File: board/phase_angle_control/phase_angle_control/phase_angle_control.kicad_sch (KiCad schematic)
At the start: 34 parts, among them J1 Screw_Terminal_01x03, J2 Conn_02x04_Odd_Even, J3 A2541HWV-7P, J4 Screw_Terminal_01x02, J6 Conn_02x04_Odd_Even, M1 MountingHoles, T1 Transformer_1P_1S, U1 STM32G030F6P, U2 EL354N(A)(TA)-VG, U3 MOC3052S-TA1, U4 ACS758xCB-050B-PFF

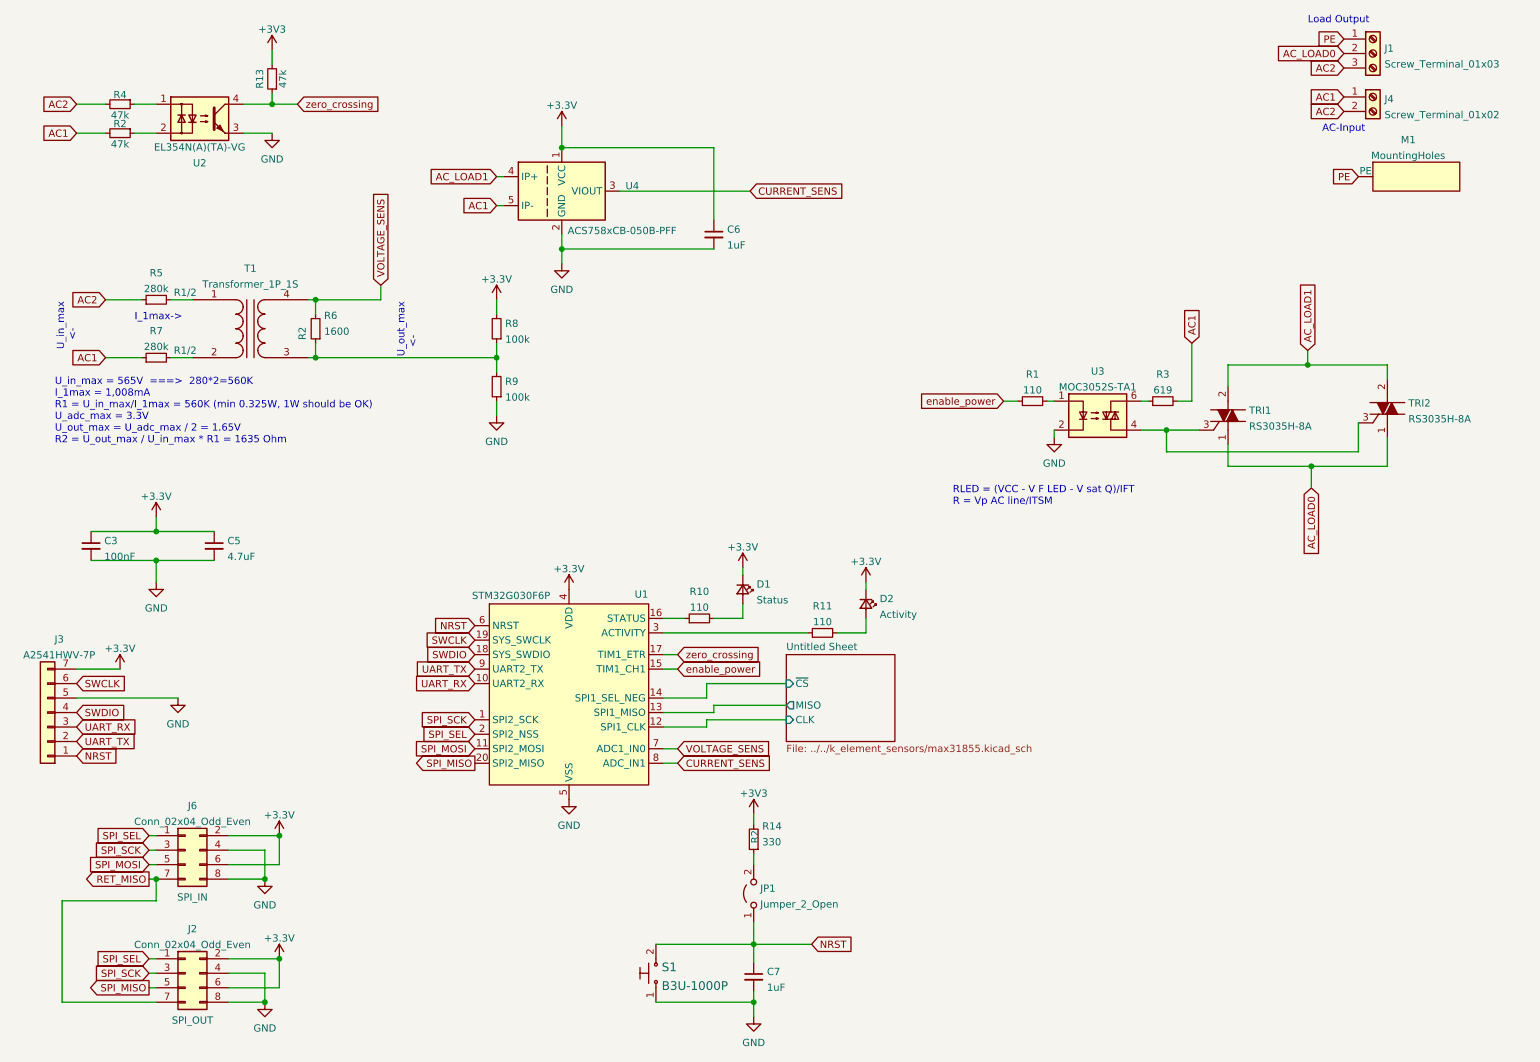
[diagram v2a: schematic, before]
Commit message: Fix LED rotation
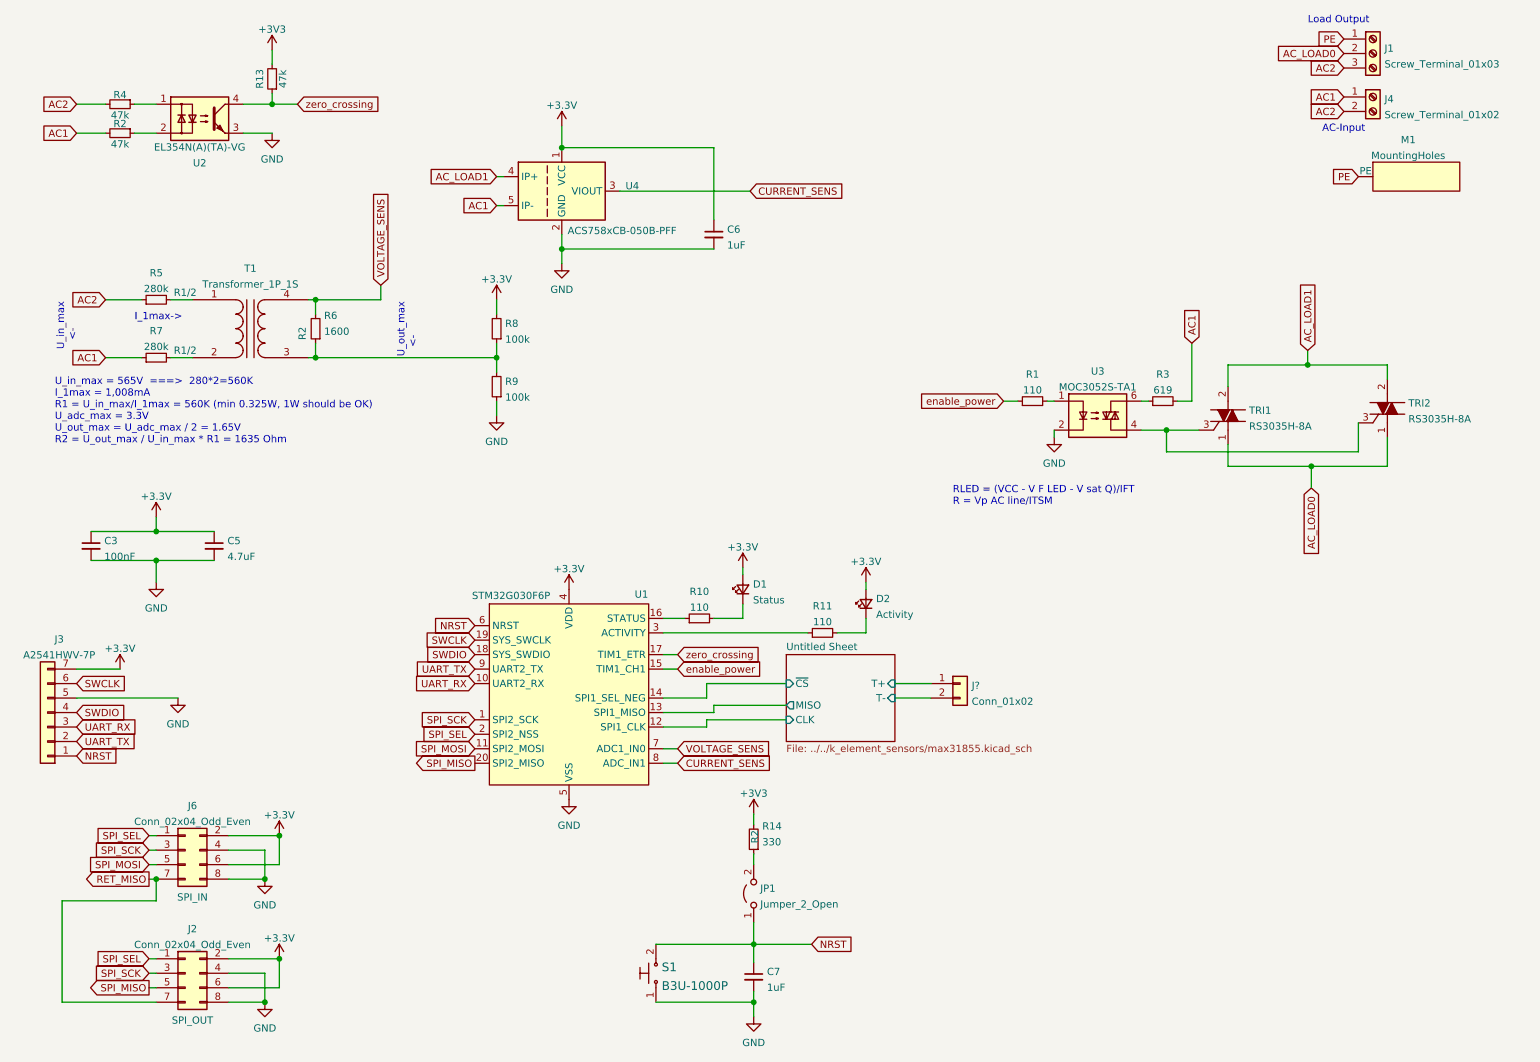
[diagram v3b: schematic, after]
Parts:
- added J?: Conn_01x02, phase_angle_control:con_A123829-NDтАО, symbol Connector_Generic:Conn_01x02
- TRI1, TRI2: Category Discrete Semiconductor Products -> (none); Family Thyristors - TRIACs -> (none)
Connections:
- net +3V3: now also D1.2 (A), D2.2 (A); no longer D1.1 (K), D2.1 (K)
- net at R10.2: now also D1.1 (K); no longer D1.2 (A)
- net at R11.2: now also D2.1 (K); no longer D2.2 (A)
- new net Untitled Sheet/T+: J?.1 (Pin_1)
- new net Untitled Sheet/T-: J?.2 (Pin_2)
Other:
- sheet Untitled Sheet ports: added T+, T-; removed none
- moved on the sheet: D1, D2
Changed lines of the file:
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@@
+    (stroke (width 0) (type solid) (color 0 0 0 0))
+  )
+  (wire (pts (xy 173.99 130.81) (xy 180.34 130.81))
+    (stroke (width 0) (type solid) (color 0 0 0 0))
+  )
+  (wire (pts (xy 173.99 133.35) (xy 180.34 133.35))
     (stroke (width 0) (type solid) (color 0 0 0 0))
   )
@@
     (pin "2")
   )
-  (symbol (lib_id "Device:LED_Small") (at 147.32 114.3 270) (unit 1)
-    (in_bom yes) (on_board yes) (fields_autoplaced)
-    (property "Reference" "D1" (id 0) (at 149.7331 113.3915 90)
-      (effects (font (size 1.27 1.27)) (justify left))
-    )
-    (property "Value" "Status" (id 1) (at 149.7331 116.1666 90)
-      (effects (font (size 1.27 1.27)) (justify left))
+  (symbol (lib_id "Device:LED_Small") (at 147.32 114.3 90) (unit 1)
+    (in_bom yes) (on_board yes) (fields_autoplaced)
+    (property "Reference" "D1" (id 0) (at 149.0981 113.3915 90)
+      (effects (font (size 1.27 1.27)) (justify right))
+    )
+    (property "Value" "Status" (id 1) (at 149.0981 116.1666 90)
+      (effects (font (size 1.27 1.27)) (justify right))
     )
     (property "Footprint" "LED_SMD:LED_0603_1608Metric_Pad1.05x0.95mm_HandSolder" (id 2) (at 147.32 114.3 90)
@@
     (pin "2")
   )
-  (symbol (lib_id "Device:LED_Small") (at 168.91 116.84 270) (unit 1)
-    (in_bom yes) (on_board yes) (fields_autoplaced)
-    (property "Reference" "D2" (id 0) (at 171.3231 115.9315 90)
-      (effects (font (size 1.27 1.27)) (justify left))
-    )
-    (property "Value" "Activity" (id 1) (at 171.3231 118.7066 90)
-      (effects (font (size 1.27 1.27)) (justify left))
+  (symbol (lib_id "Device:LED_Small") (at 168.91 116.84 90) (unit 1)
+    (in_bom yes) (on_board yes) (fields_autoplaced)
+    (property "Reference" "D2" (id 0) (at 170.6881 115.9315 90)
+      (effects (font (size 1.27 1.27)) (justify right))
+    )
+    (property "Value" "Activity" (id 1) (at 170.6881 118.7066 90)
+      (effects (font (size 1.27 1.27)) (justify right))
     )
     (property "Footprint" "LED_SMD:LED_0603_1608Metric_Pad1.05x0.95mm_HandSolder" (id 2) (at 168.91 116.84 90)
@@
     (pin "2")
   )
+  (symbol (lib_id "Connector_Generic:Conn_01x02") (at 185.42 130.81 0) (unit 1)
+    (in_bom yes) (on_board yes) (fields_autoplaced)
+    (property "Reference" "J?" (id 0) (at 187.4521 131.1715 0)
+      (effects (font (size 1.27 1.27)) (justify left))
+    )
+    (property "Value" "Conn_01x02" (id 1) (at 187.4521 133.9466 0)
+      (effects (font (size 1.27 1.27)) (justify left))
+    )
+    (property "Footprint" "phase_angle_control:con_A123829-NDтАО" (id 2) (at 185.42 130.81 0)
+      (effects (font (size 1.27 1.27)) hide)
+    )
+    (property "Datasheet" "https://www.te.com/commerce/DocumentDelivery/DDEController?Action=srchrtrv&DocNm=2834016&DocType=Customer+Drawing&DocLang=English" (id 3) (at 185.42 130.81 0)
+      (effects (font (size 1.27 1.27)) hide)
+    )
+    (pin "1")
+    (pin "2")
+  )
   (symbol (lib_id "Connector:Screw_Terminal_01x02") (at 257.81 27.94 0) (unit 1)
     (in_bom yes) (on_board yes) (fields_autoplaced)
@@
       (effects (font (size 1.524 1.524)) (justify left) hide)
     )
-    (property "Category" "Discrete Semiconductor Products" (id 10) (at 237.49 68.58 0)
-      (effects (font (size 1.524 1.524)) (justify left) hide)
-    )
-    (property "Family" "Thyristors - TRIACs" (id 11) (at 237.49 66.04 0)
-      (effects (font (size 1.524 1.524)) (justify left) hide)
-    )
-    (property "DK_Datasheet_Link" "http://www.st.com/content/ccc/resource/technical/document/datasheet/67/06/bc/c9/35/8e/4f/ea/CD00002265.pdf/files/CD00002265.pdf/jcr:content/translations/en.CD00002265.pdf" (id 12) (at 237.49 63.5 0)
-      (effects (font (size 1.524 1.524)) (justify left) hide)
-    )
-    (property "DK_Detail_Page" "/product-detail/en/stmicroelectronics/BTA16-600BWRG/497-3122-5-ND/654430" (id 13) (at 237.49 60.96 0)
+    (property "DK_Datasheet_Link" "http://www.st.com/content/ccc/resource/technical/document/datasheet/67/06/bc/c9/35/8e/4f/ea/CD00002265.pdf/files/CD00002265.pdf/jcr:content/translations/en.CD00002265.pdf" (id 13) (at 237.49 63.5 0)
+      (effects (font (size 1.524 1.524)) (justify left) hide)
+    )
+    (property "DK_Detail_Page" "/product-detail/en/stmicroelectronics/BTA16-600BWRG/497-3122-5-ND/654430" (id 14) (at 237.49 60.96 0)
       (effects (font (size 1.524 1.524)) (justify left) hide)
     )
@@
       (effects (font (size 1.524 1.524)) (justify left) hide)
     )
-    (property "Category" "Discrete Semiconductor Products" (id 10) (at 265.43 67.31 0)
-      (effects (font (size 1.524 1.524)) (justify left) hide)
-    )
-    (property "Family" "Thyristors - TRIACs" (id 11) (at 265.43 64.77 0)
-      (effects (font (size 1.524 1.524)) (justify left) hide)
-    )
-    (property "DK_Datasheet_Link" "http://www.st.com/content/ccc/resource/technical/document/datasheet/67/06/bc/c9/35/8e/4f/ea/CD00002265.pdf/files/CD00002265.pdf/jcr:content/translations/en.CD00002265.pdf" (id 12) (at 265.43 62.23 0)
-      (effects (font (size 1.524 1.524)) (justify left) hide)
-    )
-    (property "DK_Detail_Page" "/product-detail/en/stmicroelectronics/BTA16-600BWRG/497-3122-5-ND/654430" (id 13) (at 265.43 59.69 0)
+    (property "DK_Datasheet_Link" "http://www.st.com/content/ccc/resource/technical/document/datasheet/67/06/bc/c9/35/8e/4f/ea/CD00002265.pdf/files/CD00002265.pdf/jcr:content/translations/en.CD00002265.pdf" (id 13) (at 265.43 62.23 0)
+      (effects (font (size 1.524 1.524)) (justify left) hide)
+    )
+    (property "DK_Detail_Page" "/product-detail/en/stmicroelectronics/BTA16-600BWRG/497-3122-5-ND/654430" (id 14) (at 265.43 59.69 0)
       (effects (font (size 1.524 1.524)) (justify left) hide)
     )
@@
       (effects (font (size 1.27 1.27)) hide)
     )
-    (property "Datasheet" "" (id 3) (at 116.84 115.57 0)
+    (property "Datasheet" "https://www.st.com/resource/en/reference_manual/rm0454-stm32g0x0-advanced-armbased-32bit-mcus-stmicroelectronics.pdf" (id 3) (at 116.84 115.57 0)
       (effects (font (size 1.27 1.27)) hide)
     )
@@
       (effects (font (size 1.27 1.27)) (justify left))
     )
+    (pin "T+" input (at 173.99 130.81 0)
+      (effects (font (size 1.27 1.27)) (justify right))
+    )
+    (pin "T-" input (at 173.99 133.35 0)
+      (effects (font (size 1.27 1.27)) (justify right))
+    )
   )
   (sheet_instances
@@
       (reference "J6") (unit 1) (value "Conn_02x04_Odd_Even") (footprint "Connector_PinHeader_2.54mm:PinHeader_2x04_P2.54mm_Horizontal")
     )
-    (path "/aaee4988-a70a-46a5-b448-e9aacda0bab4/00000000-0000-0000-0000-0000606b809e"
-      (reference "J9") (unit 1) (value "1-2834016-2 ") (footprint "pac:con_A123829-ND‎")
+    (path "/00a2032a-bfb4-487b-92a9-8151d6a98955"
+      (reference "J?") (unit 1) (value "Conn_01x02") (footprint "phase_angle_control:con_A123829-NDтАО")
     )
     (path "/ab6c1b1a-b2ea-492e-b731-3cb1759209d9"
